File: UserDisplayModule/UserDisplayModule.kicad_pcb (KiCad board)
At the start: 2 copper layers, 187.1 x 88 mm, 157 parts, among them J1 RJ45_Shielded, U1 74HC595, U2 LM324, U3 74HC595, U4 74HC595, U5 74HC595, U6 74HC595, U7 74HC595, U8 LM7805_TO220

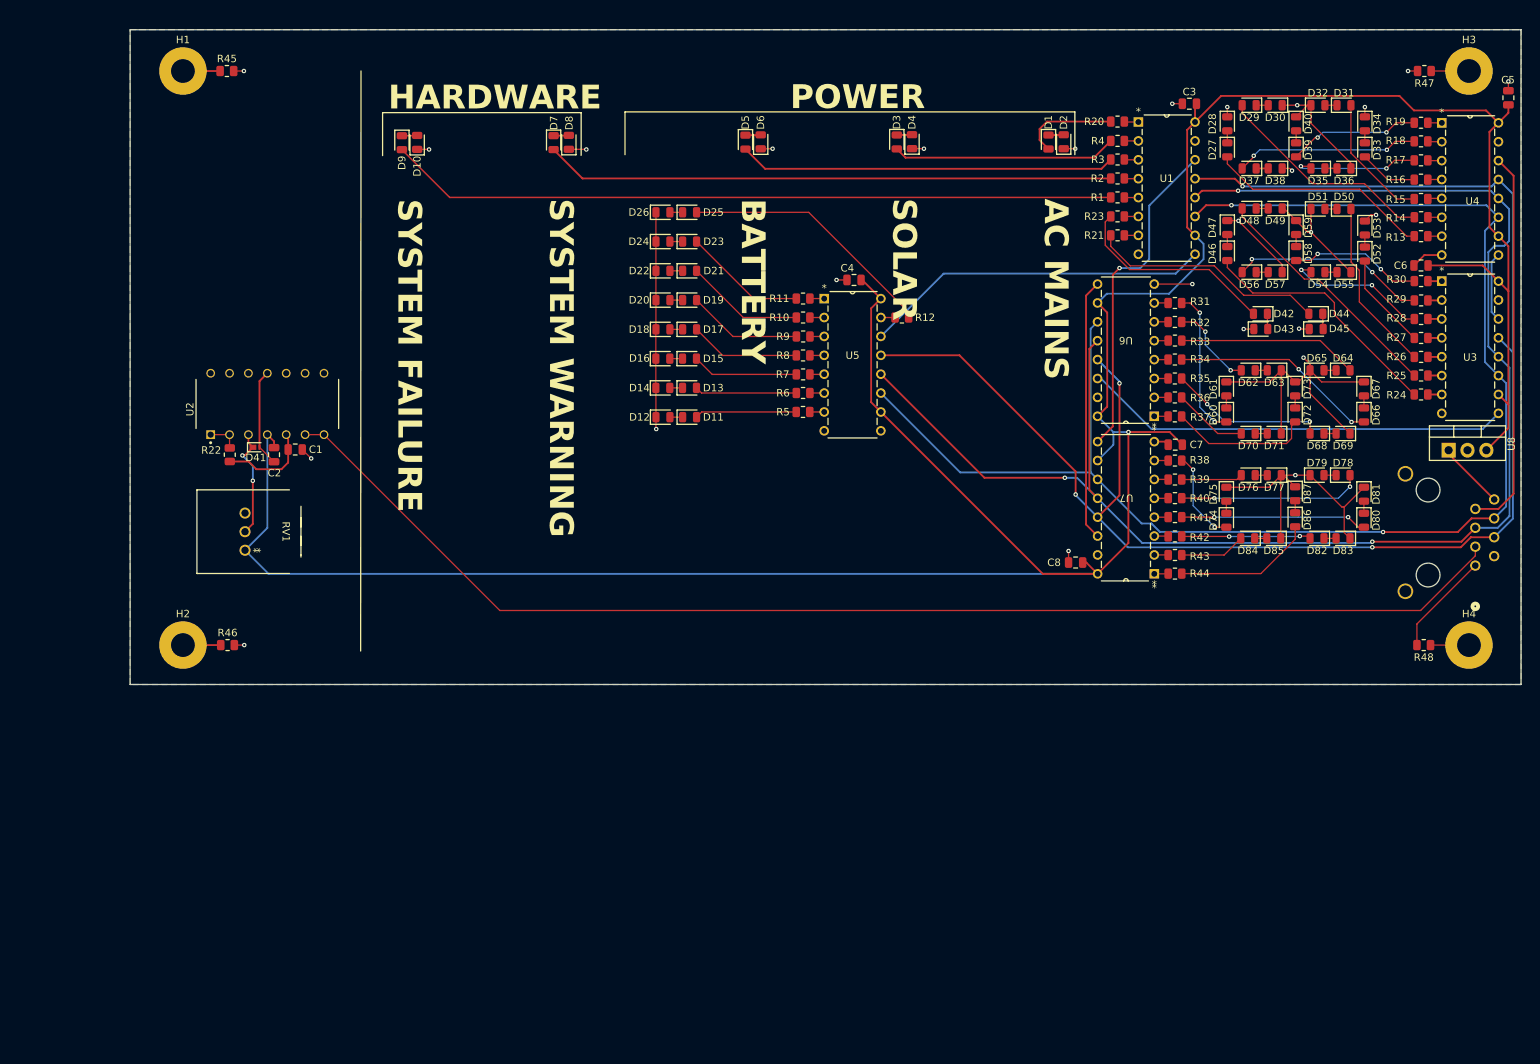
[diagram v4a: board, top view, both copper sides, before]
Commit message: added 3d models, fixed footprints, finished routing
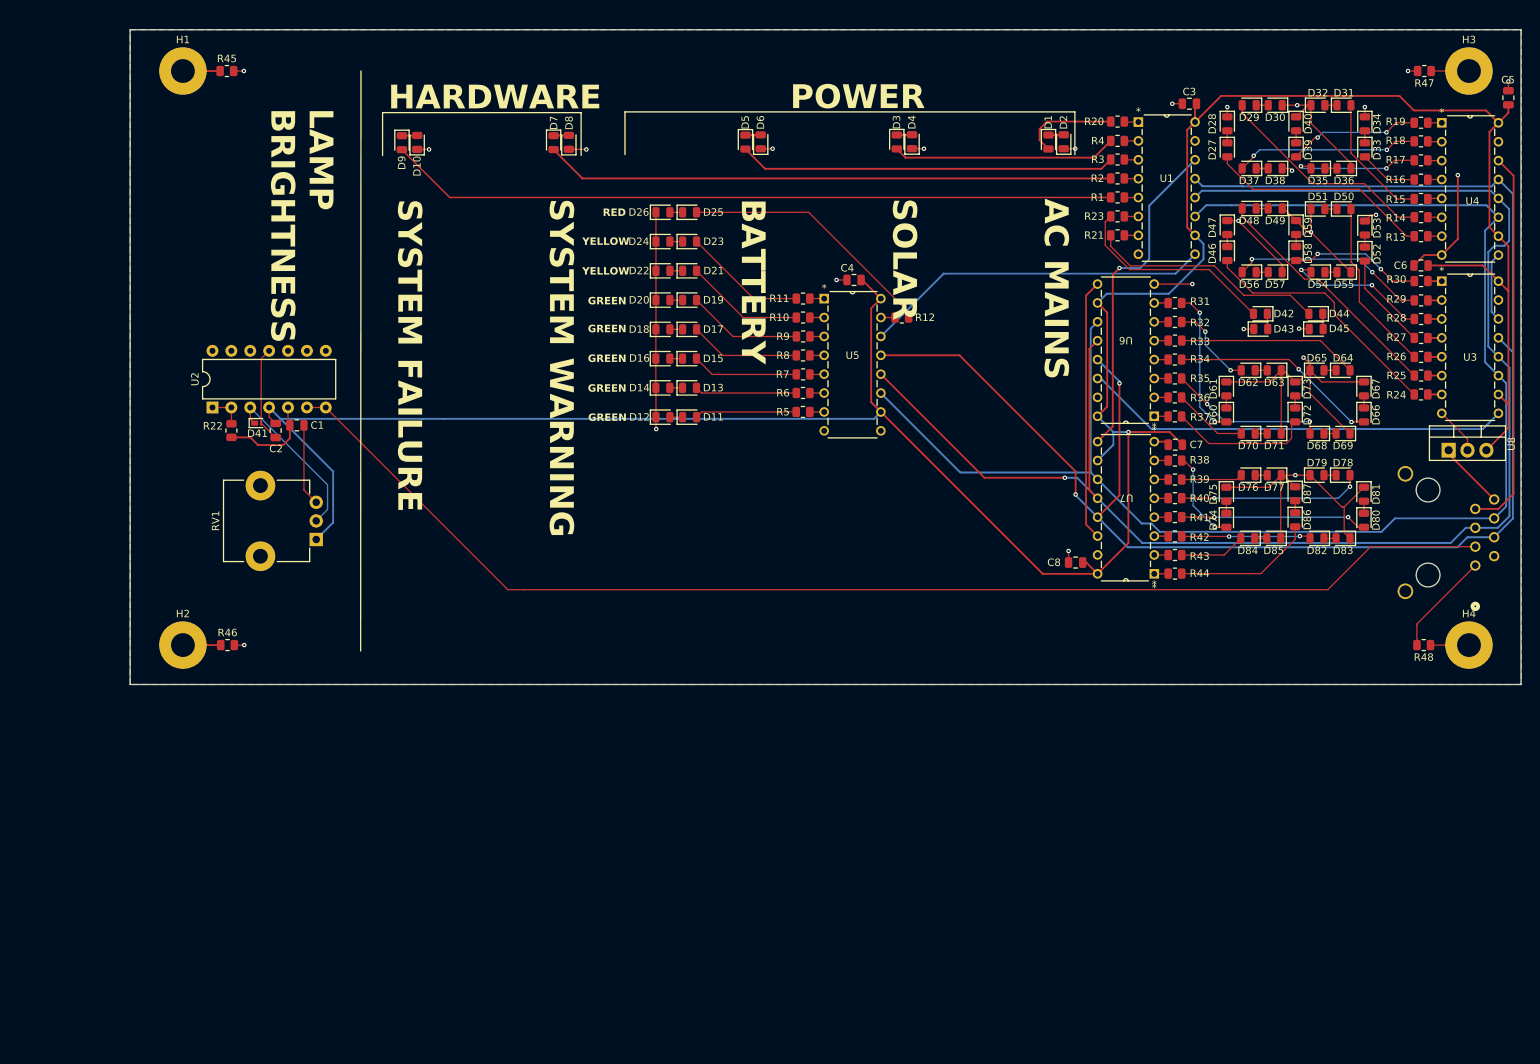
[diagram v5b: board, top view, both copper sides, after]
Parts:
- C2, C3, C4, C5, C6, C7, C8: value C -> 100nF
- RV1: footprint Potentiometer_THT:Potentiometer_Rotary -> Potentiometer_THT:Potentiometer_TT_P0915N
- U2: footprint ImportedFootprints:LM324N -> Package_DIP:DIP-14_W7.62mm
- moved RV1 9.68 mm to (65.5, 95.5), turned to 90 degrees
- moved U2 7.39 mm to (51.5, 77.8)
- moved C1 3.26 mm to (62.9, 80.2)
- moved C2 3.26 mm to (60.0, 80.8)
- moved D41 3.26 mm to (57.5, 79.8)
- moved R22 3.26 mm to (54.1, 80.8)
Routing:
- net 5V: track 397.7 -> 368.7 mm
- net GND: track 220.5 -> 247.7 mm
- net Net-(D41-K): track 15.1 -> 22.5 mm, vias 2 -> 0
- net /Brightness Dial/Brightness: track 171.4 -> 169.8 mm
- net SRCLK: vias 2 -> 0
- net RCLK: vias 3 -> 1
- net OE: vias 4 -> 2
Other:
- board text added: "GREEN"
- board text added: "LAMP BRIGHTNESS"
- board text added: "RED"
- board text added: "YELLOW"

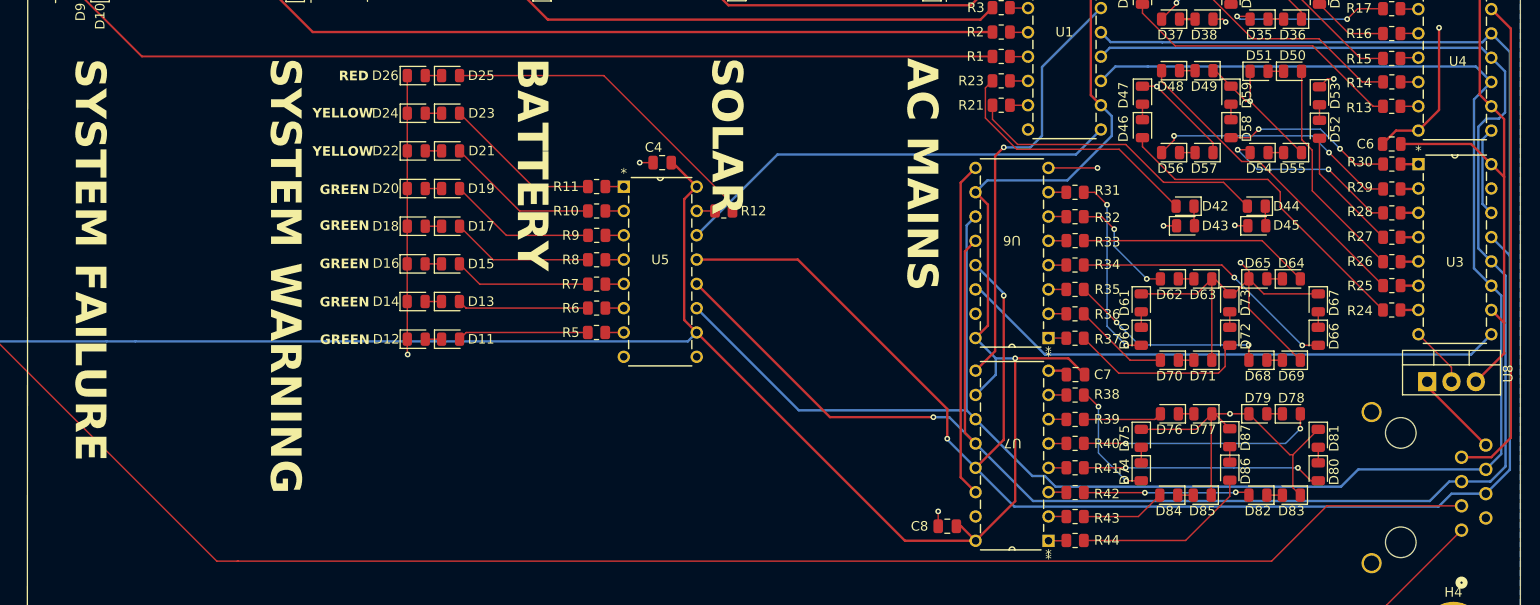
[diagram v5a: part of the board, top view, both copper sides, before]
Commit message: added digikey pns
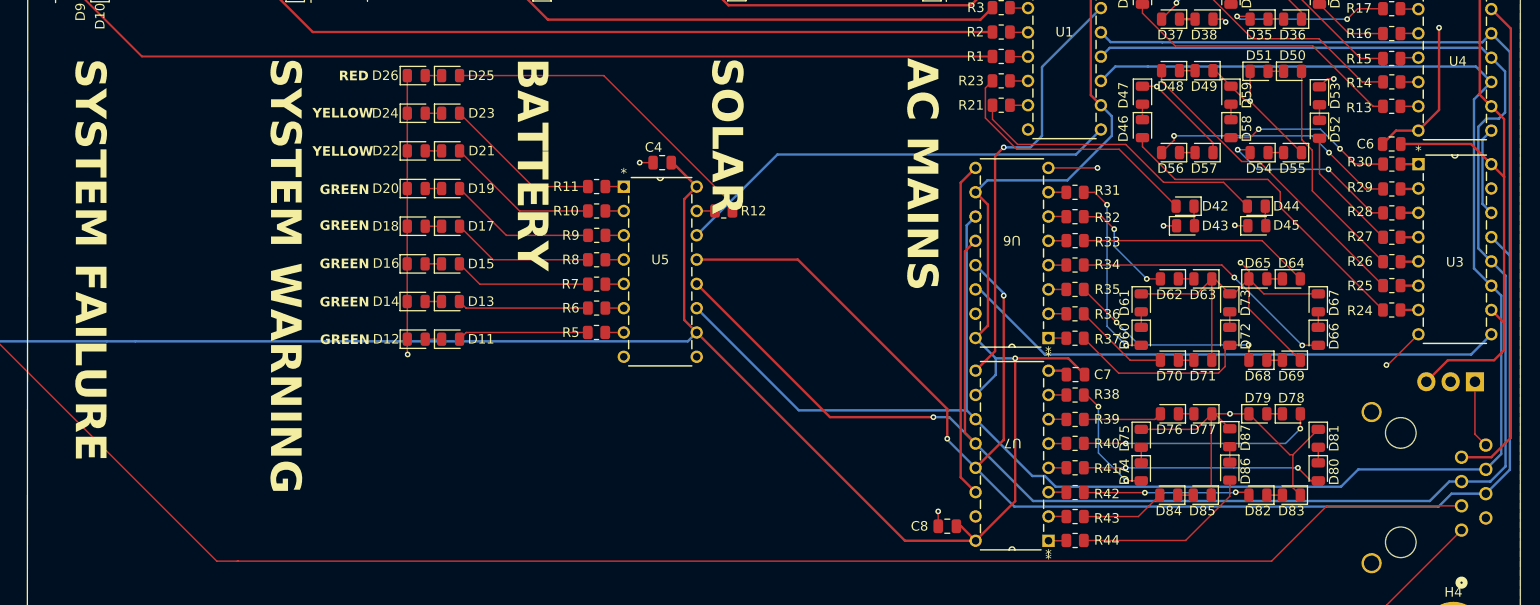
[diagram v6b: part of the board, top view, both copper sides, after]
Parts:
- U8: moved to B.Cu
- moved U8 4.99 mm to (222.8, 83.5), turned to 180 degrees
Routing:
- net 5V: track 368.7 -> 373.7 mm
- net Net-(U8-VI): track 9.16 -> 7.09 mm
- net GND: track 247.7 -> 245.9 mm, vias 26 -> 27
